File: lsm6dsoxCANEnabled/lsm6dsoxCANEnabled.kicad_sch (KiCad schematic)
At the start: 35 parts, among them J2 GPIO, J3 Power, J4 SWD, J5 CANH and CANL input n output, SW1 Nrst, SW2 BOOT0, U2 TJA1051T, U3 STM32F103C8Tx, U4 AMS1117CD-3.3, Y1 Crystal_GND24

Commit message: added finishing touches to the rev 2 design
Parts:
- added J1: Termination Resistor, Connector_PinHeader_2.54mm:PinHeader_1x02_P2.54mm_Vertical, symbol Connector:Conn_01x02_Pin
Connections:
- net CAN+: now also J1.2 (Pin_2)
- net CAN-: now also J1.1 (Pin_1)
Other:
- moved on the sheet: R4, U2

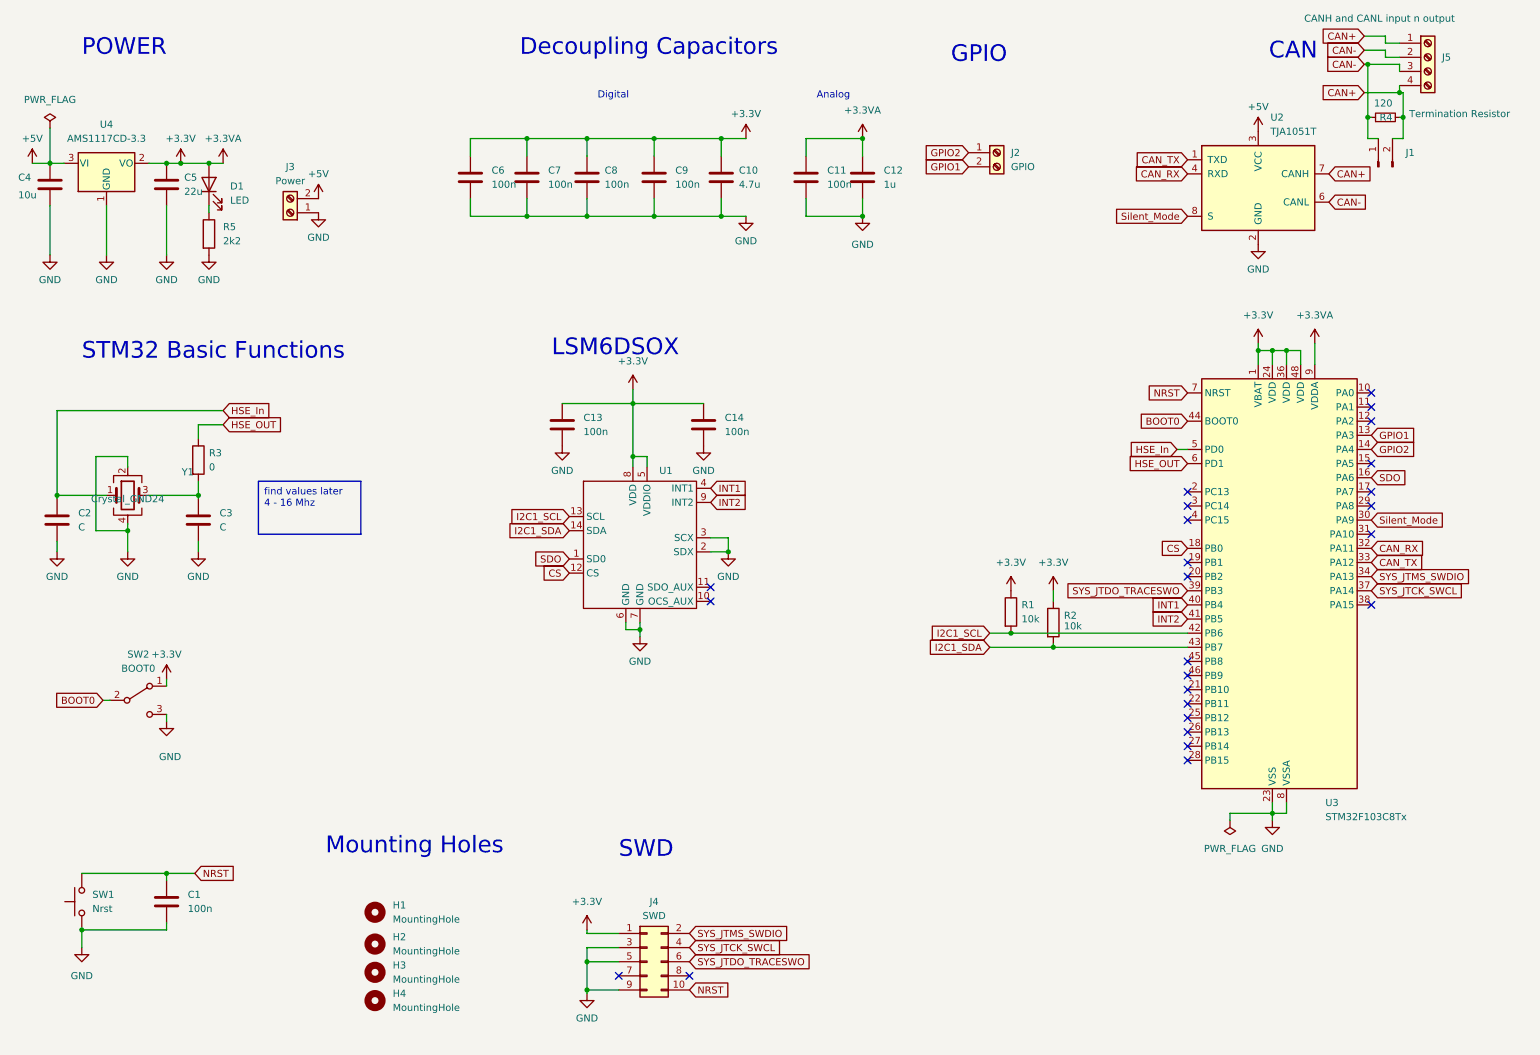
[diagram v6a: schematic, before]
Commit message: redid the traces for the LSM6DSOX CAN PCB. Also created the BOM and the CPL files for manufacturing. Which means this board should be ready to get sent to pcb manufacturing.
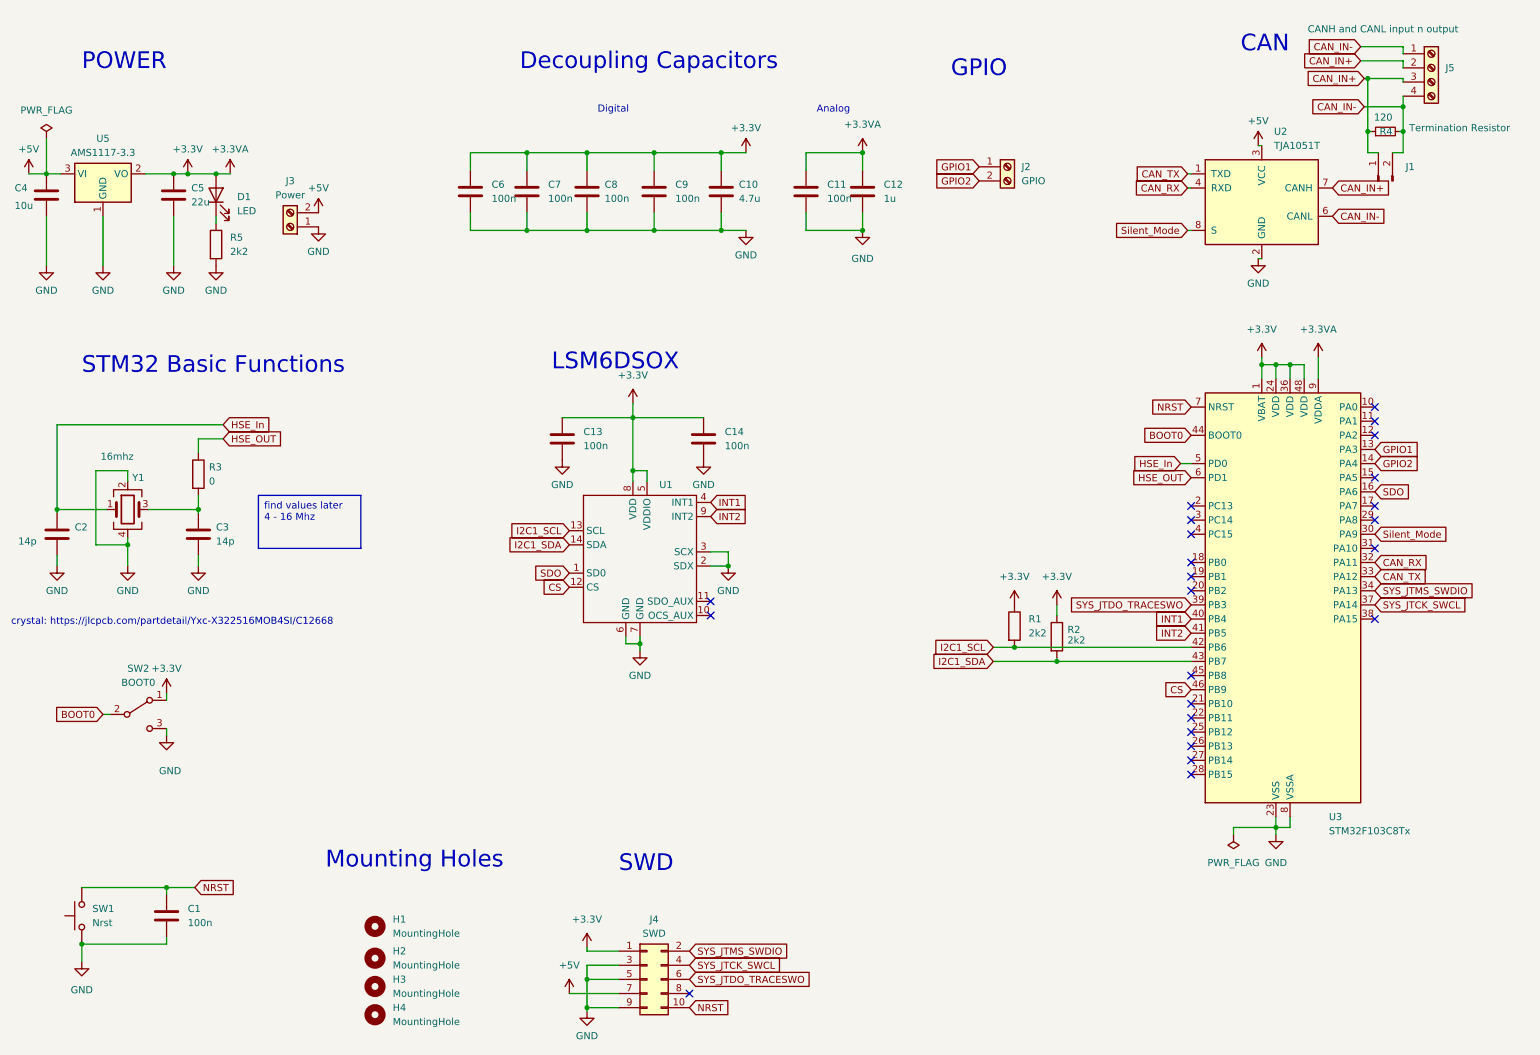
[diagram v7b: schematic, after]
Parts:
- removed U4: AMS1117CD-3.3, Package_TO_SOT_SMD:TO-252-3_TabPin2, symbol Regulator_Linear:AMS1117CD-3.3
- added U5: AMS1117-3.3, Package_TO_SOT_SMD:SOT-223-3_TabPin2, symbol Regulator_Linear:AMS1117-3.3
- C2, C3: value C -> 14p
- C5: footprint Capacitor_SMD:C_0603_1608Metric_Pad1.08x0.95mm_HandSolder -> Capacitor_SMD:C_0805_2012Metric_Pad1.18x1.45mm_HandSolder
- R1, R2: value 10k -> 2k2
- Y1: value Crystal_GND24 -> 16mhz
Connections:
- net +3.3V: now also U5.2 (VO)
- net +5V: now also J4.7 (Pin_7), U5.3 (VI)
- net CS: now also U3.46 (PB9); no longer U3.18 (PB0)
- net GND: now also U5.1 (GND)
- net GPIO1: now also J2.1 (Pin_1); no longer J2.2 (Pin_2)
- net GPIO2: now also J2.2 (Pin_2); no longer J2.1 (Pin_1)
- net CAN+ renamed CAN_IN-
- net CAN_IN-: now also U2.6 (CANL); no longer U2.7 (CANH)
- net CAN- renamed CAN_IN+
- net CAN_IN+: now also U2.7 (CANH); no longer U2.6 (CANL)
- no-connect marks 25 -> 24
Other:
- note added: "crystal: https://jlcpcb.com/partdetail/Yxc-X322516MOB4SI/C12668"
- moved on the sheet: C1, C10, C11, C12, C13, C14, C2, C3, C4, C5, C6, C7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
